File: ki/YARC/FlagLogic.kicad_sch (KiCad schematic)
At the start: 13 parts, among them U105 74LS86, U106 74LS139, U107 74HC00, U108 74HC02, U109 74LS32, U110 74LS21, U111 74LS153, U112 74LS573, U113 74LS573, U114 74LS574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

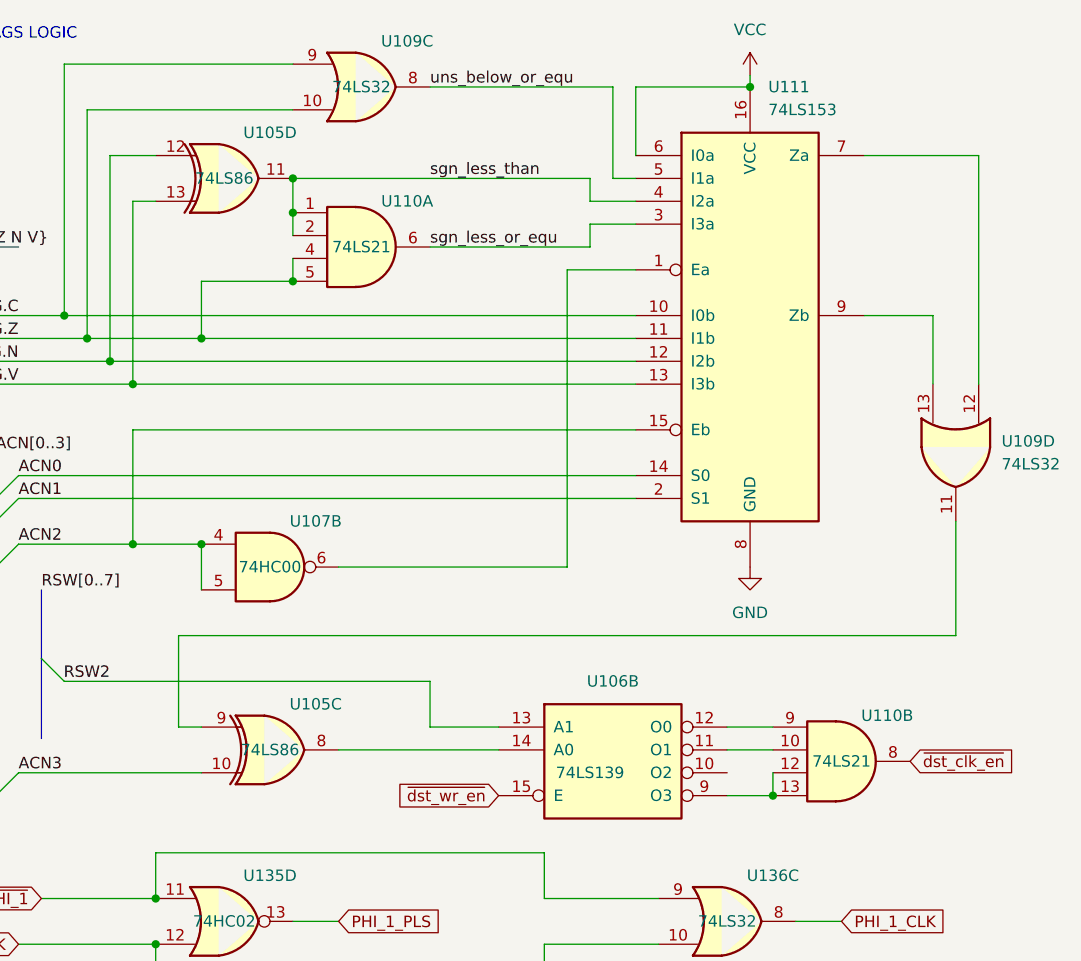
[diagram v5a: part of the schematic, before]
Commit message: Additional corrections found during wiring
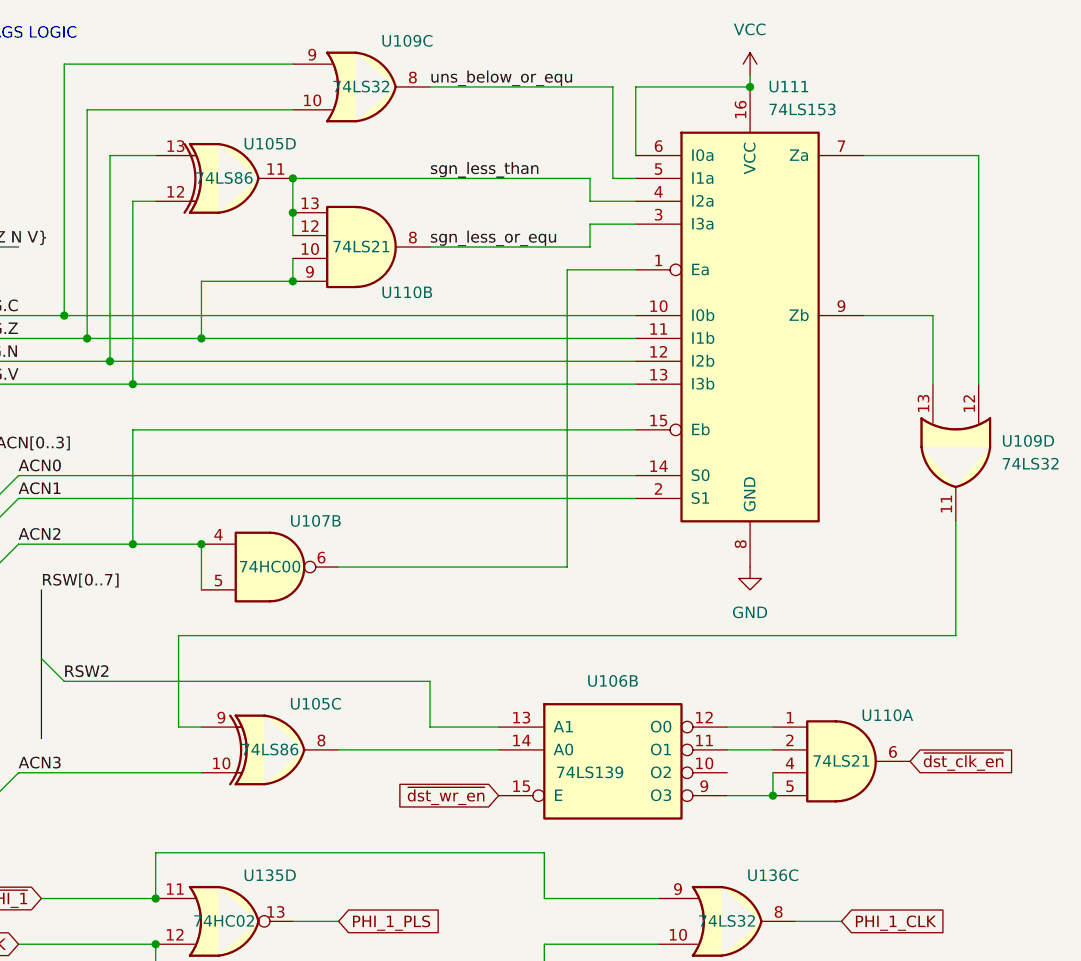
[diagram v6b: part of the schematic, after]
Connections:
- net FREG.N: now also U105.13; no longer U105.12
- net FREG.V: now also U105.12; no longer U105.13
- net FREG.Z: now also U110.10, U110.9; no longer U110.4, U110.5
- net sgn_less_or_equ: now also U110.8; no longer U110.6
- net sgn_less_than: now also U110.12, U110.13; no longer U110.1, U110.2
- net ~{dst_clk_en}: now also U110.6; no longer U110.8
- net at U106.11 (O1): now also U110.2; no longer U110.10
- net at U106.12 (O0): now also U110.1; no longer U110.9
- new net: U106.9 (O3), U110.4, U110.5
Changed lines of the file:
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@@
     (pin "1")
   )
-  (symbol (lib_id "74xx:74LS86") (at 48.26 30.48 0) (unit 4)
+  (symbol (lib_id "74xx:74LS86") (at 48.26 30.48 0) (mirror x) (unit 4)
     (in_bom yes) (on_board yes)
-    (property "Reference" "U105" (id 0) (at 53.34 25.4 0))
+    (property "Reference" "U105" (id 0) (at 53.34 26.67 0))
     (property "Value" "74LS86" (id 1) (at 48.26 30.48 0))
     (property "Footprint" "" (id 2) (at 48.26 30.48 0)
@@
     (pin "13")
   )
-  (symbol (lib_id "74xx:74LS21") (at 116.84 95.25 0) (unit 2)
+  (symbol (lib_id "74xx:74LS21") (at 116.84 95.25 0) (unit 1)
     (in_bom yes) (on_board yes)
     (property "Reference" "U110" (id 0) (at 121.92 90.17 0))
@@
       (effects (font (size 1.27 1.27)) hide)
     )
-    (pin "10")
-    (pin "12")
-    (pin "13")
-    (pin "8")
-    (pin "9")
+    (pin "1")
+    (pin "2")
+    (pin "4")
+    (pin "5")
+    (pin "6")
   )
-  (symbol (lib_id "74xx:74LS21") (at 63.5 38.1 0) (unit 1)
+  (symbol (lib_id "74xx:74LS21") (at 63.5 38.1 0) (mirror x) (unit 2)
     (in_bom yes) (on_board yes)
-    (property "Reference" "U110" (id 0) (at 68.58 33.02 0))
+    (property "Reference" "U110" (id 0) (at 68.58 43.18 0))
     (property "Value" "74LS21" (id 1) (at 63.5 38.1 0))
     (property "Footprint" "" (id 2) (at 63.5 38.1 0)
@@
       (effects (font (size 1.27 1.27)) hide)
     )
-    (pin "1")
-    (pin "2")
-    (pin "4")
-    (pin "5")
-    (pin "6")
+    (pin "10")
+    (pin "12")
+    (pin "13")
+    (pin "8")
+    (pin "9")
   )
   (symbol (lib_id "74xx:74LS32") (at 104.14 113.03 0) (unit 3)

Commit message: Condition and ALU control wiring complete.
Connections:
- net ~{dst_clk_en} renamed ~{DST_EN}
- net ~{dst_wr_en} renamed ~{DST_WRI_EN} = K:8
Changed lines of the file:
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@@
     )
   )
-  (global_label "~{dst_wr_en}" (shape input) (at 78.74 99.06 180) (fields_autoplaced)
+  (global_label "~{DST_WRI_EN} = K:8" (shape input) (at 78.74 99.06 180) (fields_autoplaced)
     (effects (font (size 1.27 1.27)) (justify right))
-    (property "Intersheet References" "${INTERSHEET_REFS}" (id 0) (at 67.1345 98.9806 0)
+    (property "Intersheet References" "${INTERSHEET_REFS}" (id 0) (at 58.5469 98.9806 0)
       (effects (font (size 1.27 1.27)) (justify right) hide)
     )
@@
     )
   )
-  (global_label "~{dst_clk_en}" (shape input) (at 124.46 95.25 0) (fields_autoplaced)
+  (global_label "~{DST_EN}" (shape input) (at 124.46 95.25 0) (fields_autoplaced)
     (effects (font (size 1.27 1.27)) (justify left))
-    (property "Intersheet References" "${INTERSHEET_REFS}" (id 0) (at 136.7307 95.1706 0)
+    (property "Intersheet References" "${INTERSHEET_REFS}" (id 0) (at 133.7674 95.1706 0)
       (effects (font (size 1.27 1.27)) (justify left) hide)
     )

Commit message: Implement run and stop COST serial commands. Correct SetK serial command. Remove unimplemeted stop and start clock serial commands. Protocol now version 7. Minor changes to hardware design.
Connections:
- net S2_LD_CLK: no longer U113.11 (Load)
- net S2_LD_PLS: now also U113.11 (Load)
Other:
- note added: "ALU INPUT AND OUTPUT CONTROLS LOCATED IN FLAGS"
- note removed: "ALU INPUT AND OUTPUT CONTROLS LOCATED IN ALU"
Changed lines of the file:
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@@
     (stroke (width 0) (type default) (color 0 0 0 0))
   )
-  (text "ALU INPUT AND\nOUTPUT CONTROLS\nLOCATED IN ALU" (at 16.51 130.81 0)
+  (text "ALU INPUT AND\nOUTPUT CONTROLS\nLOCATED IN FLAGS" (at 16.51 130.81 0)
     (effects (font (size 1.27 1.27)) (justify left bottom))
   )
@@
     )
   )
-  (global_label "S2_LD_CLK" (shape input) (at 193.04 104.14 90) (fields_autoplaced)
+  (global_label "S2_LD_PLS" (shape input) (at 193.04 104.14 90) (fields_autoplaced)
     (effects (font (size 1.27 1.27)) (justify left))
-    (property "Intersheet References" "${INTERSHEET_REFS}" (id 0) (at 192.9606 91.5064 90)
+    (property "Intersheet References" "${INTERSHEET_REFS}" (id 0) (at 192.9606 91.5669 90)
       (effects (font (size 1.27 1.27)) (justify left) hide)
     )
